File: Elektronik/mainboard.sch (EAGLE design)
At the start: 35 parts, among them IC1 TXS0102DCU, IC2 SP6201EM5-L-3-3, IC3 SRV05-4.TCT, X2 USB-MINI32005-601, X4 MICROMATCH-8-WEIBLICH

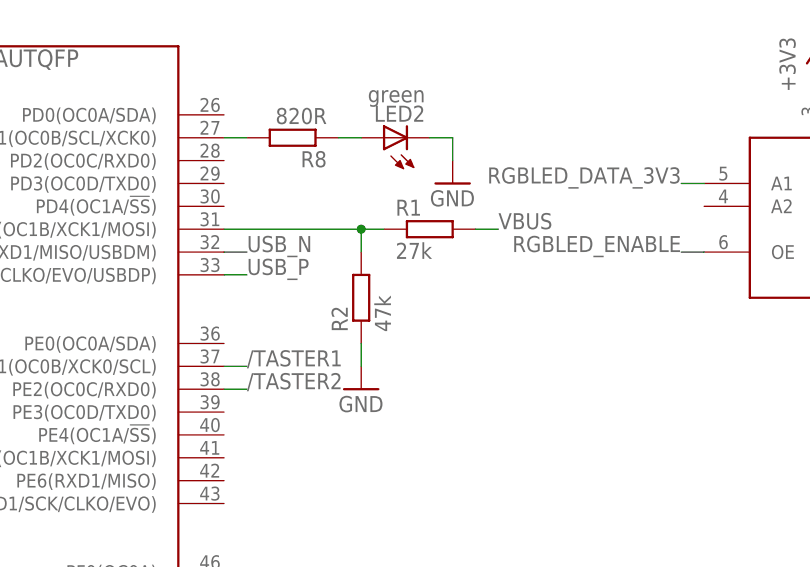
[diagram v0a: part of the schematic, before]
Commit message: [Elektronik] Spannungsteiler für VBUS angepasst, damit die Pullups der Datenleitungen die VBUS-leitung nicht über die ESD-Dioden nach oben ziehen
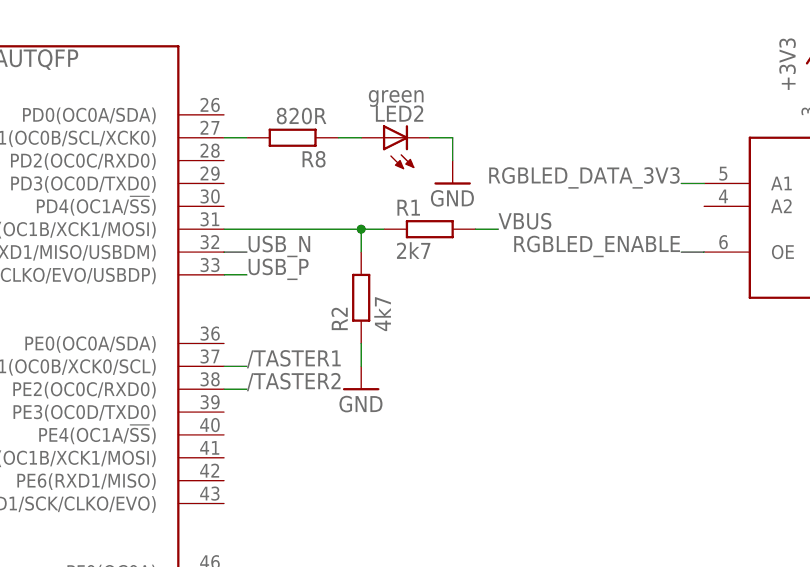
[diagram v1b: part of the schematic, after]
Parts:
- R1: value 27k -> 2k7
- R2: value 47k -> 4k7
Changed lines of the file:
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@@
 <part name="IC3" library="TURAG_Diode" deviceset="SRV05-4" device=".TCT"/>
 <part name="GND7" library="supply1" deviceset="GND" device=""/>
-<part name="R1" library="rcl" deviceset="R-EU_" device="R0603" value="27k"/>
-<part name="R2" library="rcl" deviceset="R-EU_" device="R0603" value="47k"/>
+<part name="R1" library="rcl" deviceset="R-EU_" device="R0603" value="2k7"/>
+<part name="R2" library="rcl" deviceset="R-EU_" device="R0603" value="4k7"/>
 <part name="GND8" library="supply1" deviceset="GND" device=""/>
 <part name="R3" library="rcl" deviceset="R-EU_" device="R0603" value="1M"/>

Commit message: Items sind jetzt alle selectable
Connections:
- net /RESET renamed !RESET!
- net /TASTER1 renamed !TASTER1!
- net /TASTER2 renamed !TASTER2!
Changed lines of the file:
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@@
 </segment>
 </net>
-<net name="/RESET" class="0">
+<net name="!RESET!" class="0">
 <segment>
 <pinref part="U$1" gate="G$1" pin="PDI-CLK/!RESET"/>
@@
 </segment>
 </net>
-<net name="/TASTER1" class="0">
+<net name="!TASTER1!" class="0">
 <segment>
 <pinref part="TA2" gate="G$1" pin="S"/>
@@
 </segment>
 </net>
-<net name="/TASTER2" class="0">
+<net name="!TASTER2!" class="0">
 <segment>
 <pinref part="TA3" gate="G$1" pin="S"/>

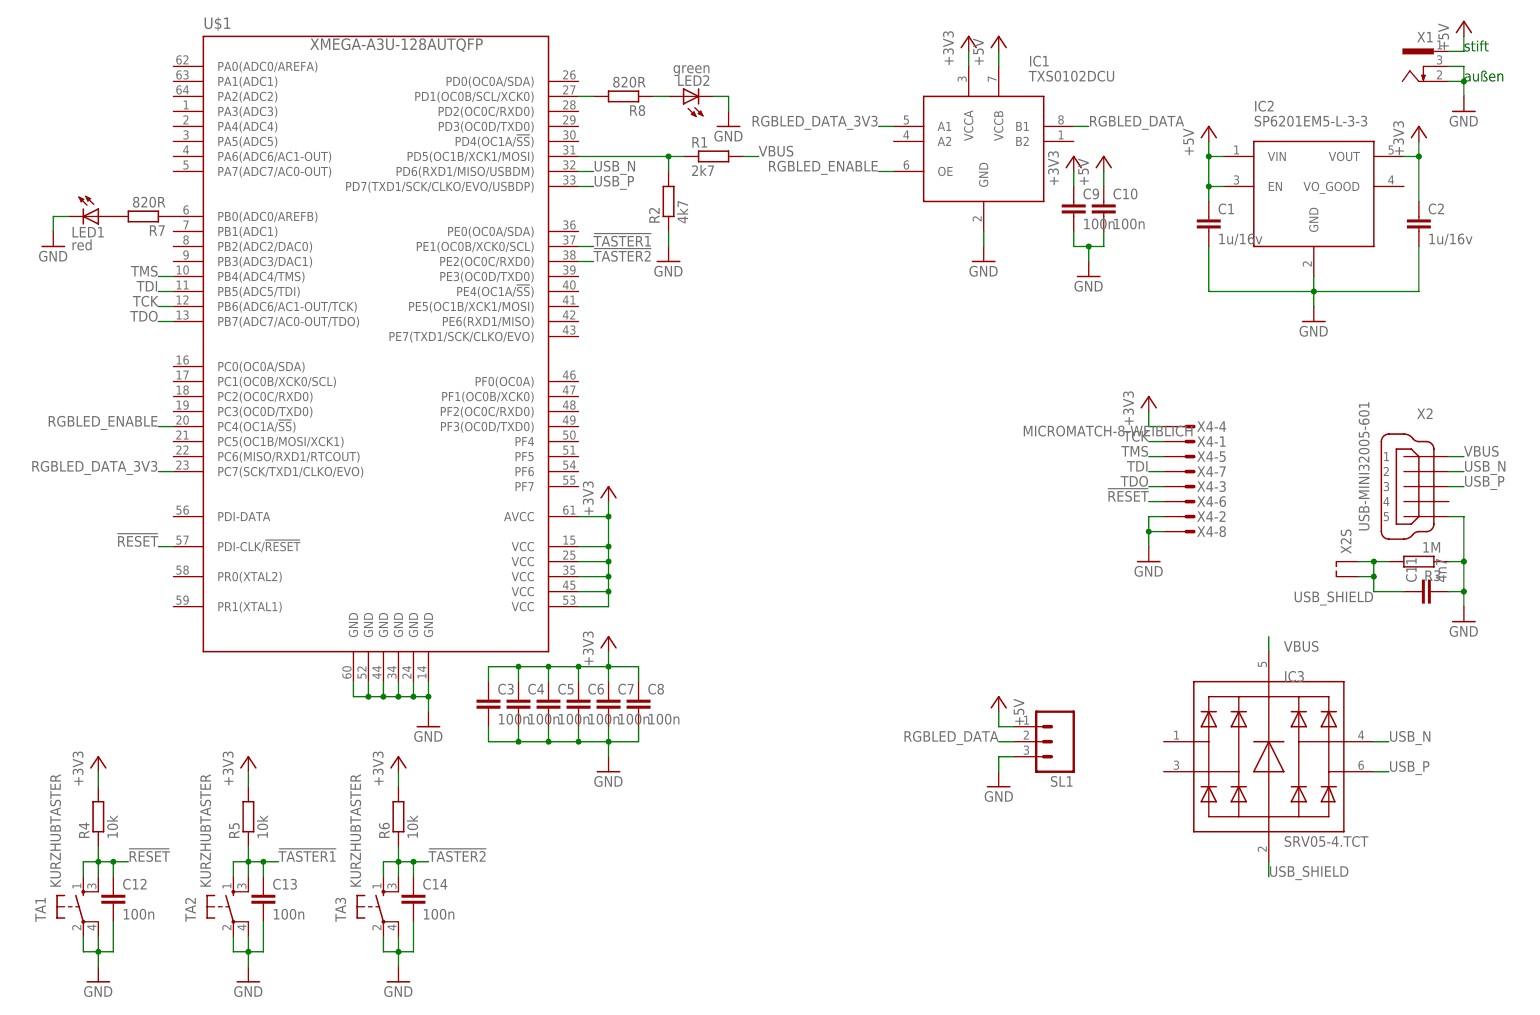
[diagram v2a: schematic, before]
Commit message: [Elektronik] Layout für Fertigung in der Uni angepasst
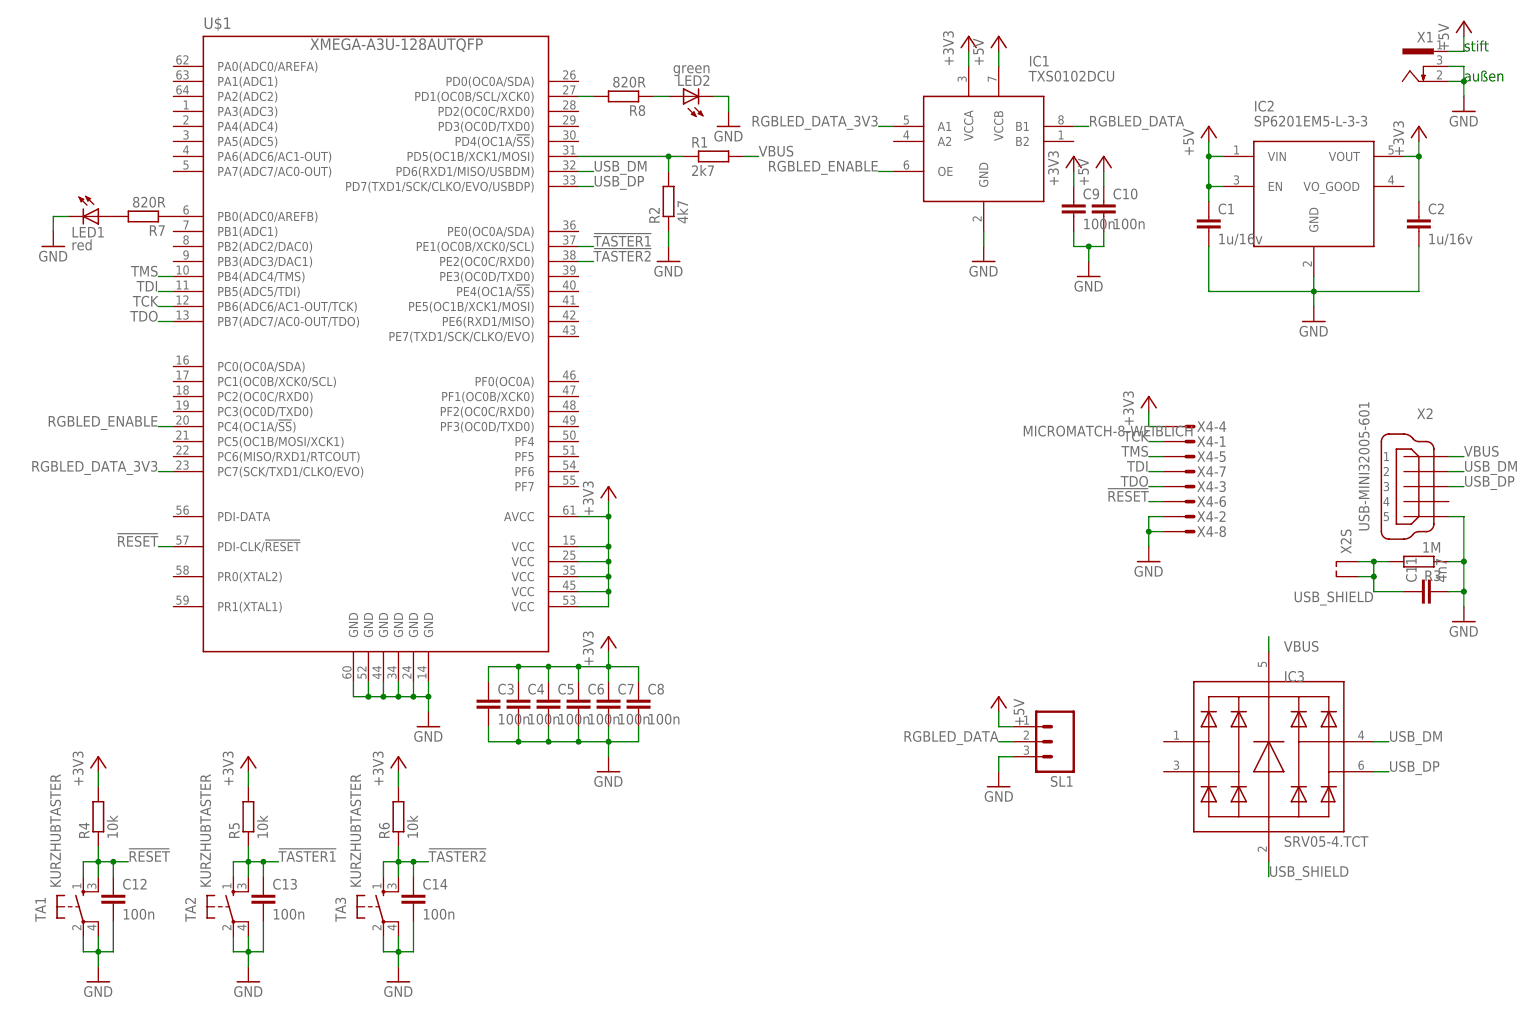
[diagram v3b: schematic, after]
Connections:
- net USB_N renamed USB_DM
- net USB_P renamed USB_DP
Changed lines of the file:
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@@
 <?xml version="1.0" encoding="utf-8"?>
 <!DOCTYPE eagle SYSTEM "eagle.dtd">
-<eagle version="6.5.0">
+<eagle version="7.1.0">
 <drawing>
 <settings>
@@
 <layer number="110" name="fp0" color="7" fill="1" visible="yes" active="yes"/>
 <layer number="111" name="LPC17xx" color="7" fill="1" visible="yes" active="yes"/>
+<layer number="112" name="tSilk" color="7" fill="1" visible="yes" active="yes"/>
 <layer number="116" name="Patch_BOT" color="7" fill="1" visible="yes" active="yes"/>
 <layer number="121" name="_tsilk" color="7" fill="1" visible="yes" active="yes"/>
@@
 <layer number="124" name="bTestmark" color="7" fill="1" visible="yes" active="yes"/>
 <layer number="125" name="_tNames" color="7" fill="1" visible="yes" active="yes"/>
+<layer number="126" name="_bNames" color="7" fill="1" visible="yes" active="yes"/>
+<layer number="127" name="_tValues" color="7" fill="1" visible="yes" active="yes"/>
+<layer number="128" name="_bValues" color="7" fill="1" visible="yes" active="yes"/>
 <layer number="131" name="tAdjust" color="7" fill="1" visible="yes" active="yes"/>
 <layer number="132" name="bAdjust" color="7" fill="1" visible="yes" active="yes"/>
 <layer number="144" name="Drill_legend" color="7" fill="1" visible="yes" active="yes"/>
+<layer number="150" name="Notes" color="7" fill="1" visible="yes" active="yes"/>
 <layer number="151" name="HeatSink" color="7" fill="1" visible="yes" active="yes"/>
+<layer number="152" name="_bDocu" color="7" fill="1" visible="yes" active="yes"/>
+<layer number="153" name="FabDoc1" color="7" fill="1" visible="yes" active="yes"/>
+<layer number="154" name="FabDoc2" color="7" fill="1" visible="yes" active="yes"/>
+<layer number="155" name="FabDoc3" color="7" fill="1" visible="yes" active="yes"/>
 <layer number="169" name="Baugruppen" color="7" fill="1" visible="yes" active="yes"/>
 <layer number="199" name="Contour" color="7" fill="1" visible="yes" active="yes"/>
@@
 <layer number="215" name="215bmp" color="7" fill="1" visible="yes" active="yes"/>
 <layer number="216" name="216bmp" color="7" fill="1" visible="yes" active="yes"/>
+<layer number="217" name="217bmp" color="7" fill="1" visible="yes" active="yes"/>
+<layer number="218" name="218bmp" color="7" fill="1" visible="yes" active="yes"/>
+<layer number="219" name="219bmp" color="7" fill="1" visible="yes" active="yes"/>
+<layer number="220" name="220bmp" color="7" fill="1" visible="yes" active="yes"/>
+<layer number="221" name="221bmp" color="7" fill="1" visible="yes" active="yes"/>
+<layer number="222" name="222bmp" color="7" fill="1" visible="yes" active="yes"/>
+<layer number="223" name="223bmp" color="7" fill="1" visible="yes" active="yes"/>
+<layer number="224" name="224bmp" color="7" fill="1" visible="yes" active="yes"/>
+<layer number="225" name="225bmp" color="7" fill="1" visible="no" active="yes"/>
+<layer number="226" name="226bmp" color="7" fill="1" visible="no" active="yes"/>
+<layer number="227" name="227bmp" color="7" fill="1" visible="no" active="yes"/>
+<layer number="228" name="228bmp" color="7" fill="1" visible="no" active="yes"/>
 <layer number="231" name="Eagle3D_PG1" color="7" fill="1" visible="yes" active="yes"/>
 <layer number="232" name="Eagle3D_PG2" color="7" fill="1" visible="yes" active="yes"/>
 <layer number="233" name="Eagle3D_PG3" color="7" fill="1" visible="yes" active="yes"/>
+<layer number="248" name="Housing" color="7" fill="1" visible="yes" active="yes"/>
+<layer number="249" name="Edge" color="7" fill="1" visible="yes" active="yes"/>
 <layer number="250" name="Descript" color="3" fill="1" visible="yes" active="yes"/>
 <layer number="251" name="SMDround" color="12" fill="11" visible="yes" active="yes"/>
@@
 </segment>
 </net>
-<net name="USB_N" class="0">
+<net name="USB_DM" class="0">
+<segment>
+<pinref part="X2" gate="G41" pin="2"/>
+<wire x1="243.84" y1="93.98" x2="246.38" y2="93.98" width="0.1524" layer="91"/>
+<label x="246.38" y="93.98" size="1.778" layer="95"/>
+</segment>
+<segment>
+<pinref part="IC3" gate="G$1" pin="3"/>
+<wire x1="231.14" y1="48.26" x2="233.68" y2="48.26" width="0.1524" layer="91"/>
+<label x="233.68" y="48.26" size="1.778" layer="95"/>
+</segment>
 <segment>
 <pinref part="U$1" gate="G$1" pin="PD6(RXD1/MISO/USBDM)"/>
@@
 <label x="99.06" y="144.78" size="1.778" layer="95"/>
 </segment>
-<segment>
-<pinref part="X2" gate="G41" pin="2"/>
-<wire x1="243.84" y1="93.98" x2="246.38" y2="93.98" width="0.1524" layer="91"/>
-<label x="246.38" y="93.98" size="1.778" layer="95"/>
-</segment>
-<segment>
-<pinref part="IC3" gate="G$1" pin="3"/>
-<wire x1="231.14" y1="48.26" x2="233.68" y2="48.26" width="0.1524" layer="91"/>
-<label x="233.68" y="48.26" size="1.778" layer="95"/>
-</segment>
 </net>
-<net name="USB_P" class="0">
+<net name="USB_DP" class="0">
 <segment>
 <pinref part="U$1" gate="G$1" pin="PD7(TXD1/SCK/CLKO/EVO/USBDP)"/>
